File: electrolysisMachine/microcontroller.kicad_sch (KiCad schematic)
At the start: 1 part

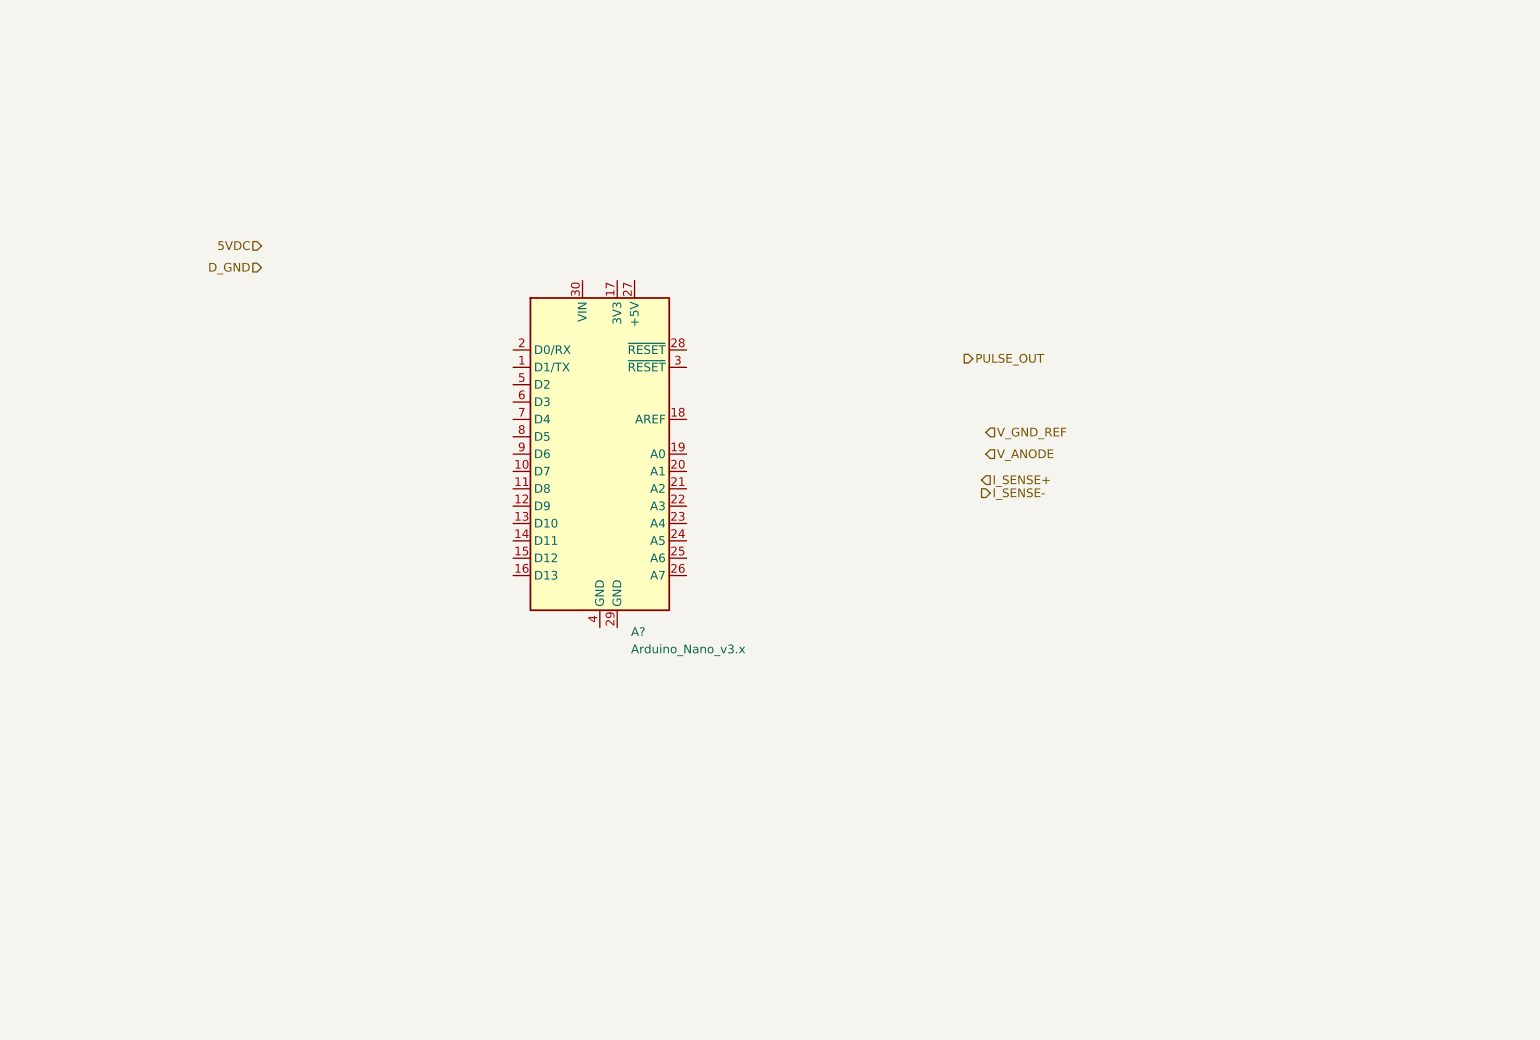
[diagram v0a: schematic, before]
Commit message: Added test circuit schematic
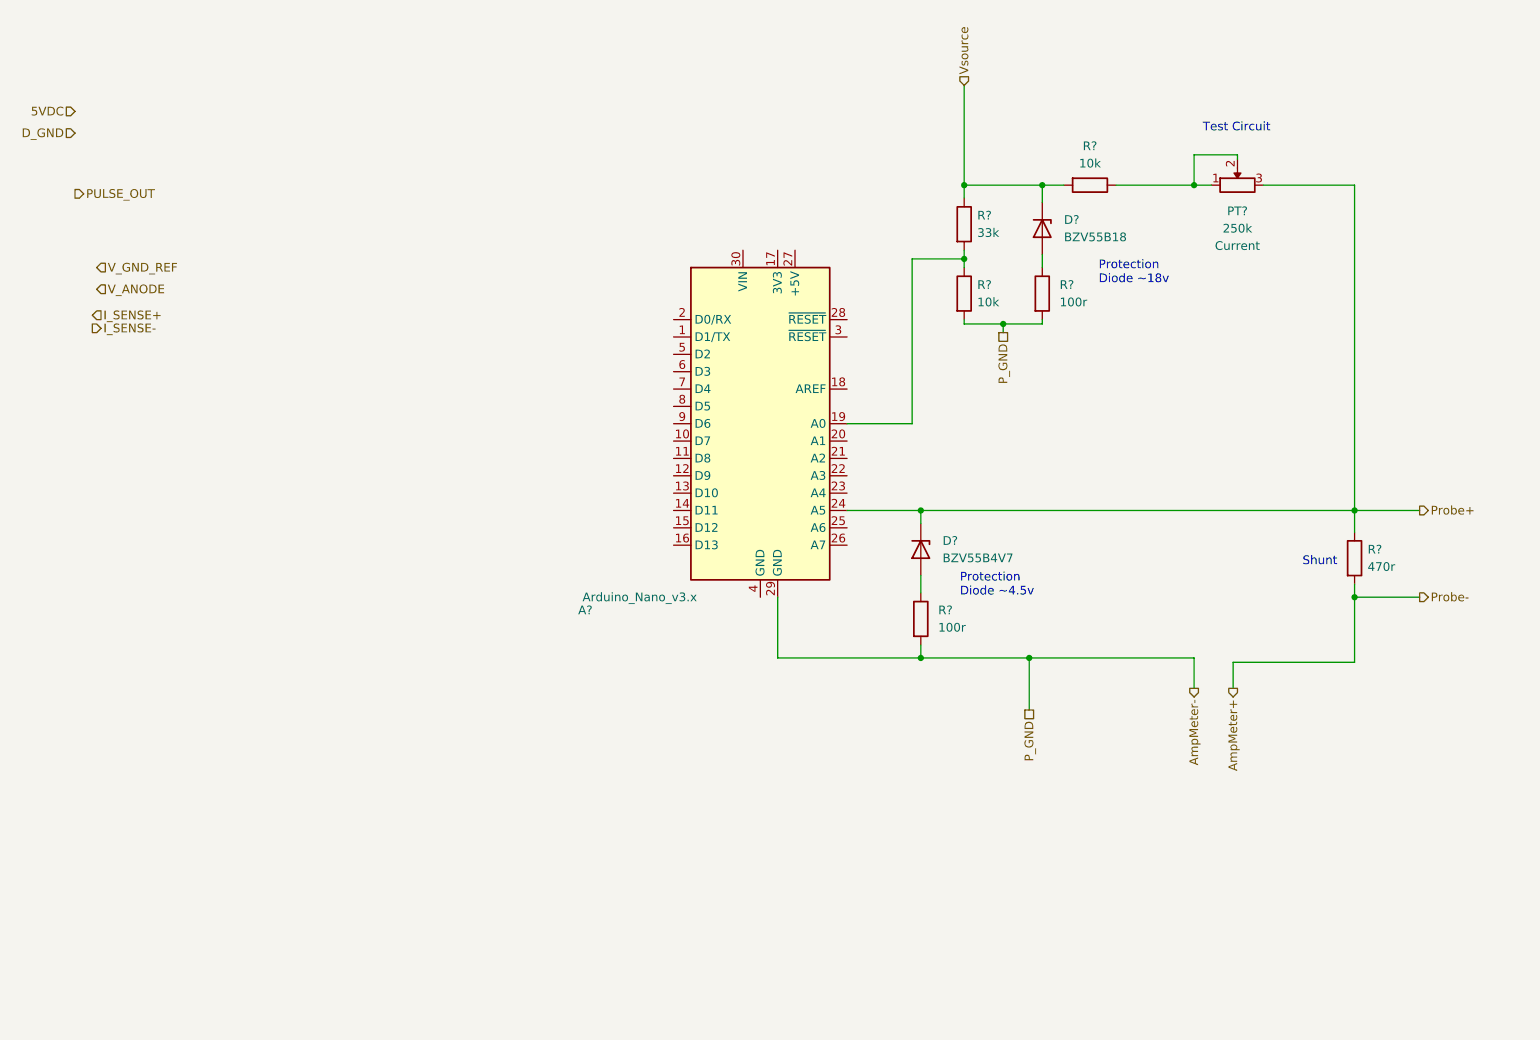
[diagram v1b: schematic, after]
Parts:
- added D?: BZV55B18, Diode_SMD:D_MiniMELF, symbol Diode:BZV55B18
- added D?: BZV55B4V7, Diode_SMD:D_MiniMELF, symbol Diode:BZV55B4V7
- added PT?: 250k, Potentiometer_THT:Potentiometer_Alpha_RD901F-40-00D_Single_Vertical_CircularHoles, symbol 000_Resistors_Immo:Potentiometer
- added R? (x2): 100r, Resistor_SMD:R_0805_2012Metric_Pad1.20x1.40mm_HandSolder, symbol 000_Resistors_Immo:Resistor_0805
- added R?: 470r, Resistor_SMD:R_0805_2012Metric_Pad1.20x1.40mm_HandSolder, symbol 000_Resistors_Immo:Resistor_0805
- added R? (x2): 10k, Resistor_SMD:R_0805_2012Metric_Pad1.20x1.40mm_HandSolder, symbol 000_Resistors_Immo:Resistor_0805
- added R?: 33k, Resistor_SMD:R_0805_2012Metric_Pad1.20x1.40mm_HandSolder, symbol 000_Resistors_Immo:Resistor_0805
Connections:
- net at A?.19 (A0): now also R?.1, R?.2
- net Probe+: now reaches A?.24 (A5)
- net Probe+: now also D?.1 (K), PT?.3, R?.1
- net AmpMeter-: now reaches A?.29 (GND)
- net AmpMeter-: now also R?.2, R?.2, R?.2
- new net: D?.2 (A), R?.1 (x2)
- new net: PT?.1, PT?.2, R?.1
- new net AmpMeter+: R?.2
- new net Vsource: D?.1 (K), R?.1, R?.2
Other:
- note added: "Protection Diode ~18v"
- note added: "Protection Diode ~4.5v"
- note added: "Shunt"
- note added: "Test Circuit"
- moved on the sheet: A?

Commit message: cgfhgfh
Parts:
- gave numbers to parts that had none: 10
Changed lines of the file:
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@@
   (symbol (lib_id "Diode:BZV55B18") (at 172.085 43.815 270) (unit 1)
     (in_bom yes) (on_board yes) (fields_autoplaced)
-    (property "Reference" "D?" (id 0) (at 175.26 42.5449 90)
+    (property "Reference" "D1" (id 0) (at 175.26 42.5449 90)
       (effects (font (size 1.27 1.27)) (justify left))
     )
@@
   (symbol (lib_id "000_Resistors_Immo:Resistor_0805") (at 172.085 53.34 270) (unit 1)
     (in_bom yes) (on_board yes) (fields_autoplaced)
-    (property "Reference" "R?" (id 0) (at 174.625 52.0699 90)
+    (property "Reference" "R4" (id 0) (at 174.625 52.0699 90)
       (effects (font (size 1.27 1.27)) (justify left))
     )
@@
   (symbol (lib_id "000_Resistors_Immo:Resistor_0805") (at 217.805 92.075 270) (unit 1)
     (in_bom yes) (on_board yes) (fields_autoplaced)
-    (property "Reference" "R?" (id 0) (at 219.71 90.8049 90)
+    (property "Reference" "R5" (id 0) (at 219.71 90.8049 90)
       (effects (font (size 1.27 1.27)) (justify left))
     )
@@
   (symbol (lib_id "000_Resistors_Immo:Resistor_0805") (at 154.305 100.965 270) (unit 1)
     (in_bom yes) (on_board yes) (fields_autoplaced)
-    (property "Reference" "R?" (id 0) (at 156.845 99.6949 90)
+    (property "Reference" "R6" (id 0) (at 156.845 99.6949 90)
       (effects (font (size 1.27 1.27)) (justify left))
     )
@@
   (symbol (lib_id "MCU_Module:Arduino_Nano_v3.x") (at 130.81 72.39 0) (unit 1)
     (in_bom yes) (on_board yes)
-    (property "Reference" "A?" (id 0) (at 104.14 99.695 0)
+    (property "Reference" "A1" (id 0) (at 104.14 99.695 0)
       (effects (font (size 1.27 1.27)) (justify left))
     )
@@
   (symbol (lib_id "000_Resistors_Immo:Resistor_0805") (at 179.07 37.465 180) (unit 1)
     (in_bom yes) (on_board yes) (fields_autoplaced)
-    (property "Reference" "R?" (id 0) (at 179.07 31.75 0))
+    (property "Reference" "R1" (id 0) (at 179.07 31.75 0))
     (property "Value" "10k" (id 1) (at 179.07 34.29 0))
     (property "Footprint" "Resistor_SMD:R_0805_2012Metric_Pad1.20x1.40mm_HandSolder" (id 2) (at 179.07 35.687 0)
@@
   (symbol (lib_id "000_Resistors_Immo:Resistor_0805") (at 160.655 43.18 270) (unit 1)
     (in_bom yes) (on_board yes) (fields_autoplaced)
-    (property "Reference" "R?" (id 0) (at 162.56 41.9099 90)
+    (property "Reference" "R2" (id 0) (at 162.56 41.9099 90)
       (effects (font (size 1.27 1.27)) (justify left))
     )
@@
   (symbol (lib_id "Diode:BZV55B4V7") (at 154.305 90.805 270) (unit 1)
     (in_bom yes) (on_board yes) (fields_autoplaced)
-    (property "Reference" "D?" (id 0) (at 157.48 89.5349 90)
+    (property "Reference" "D2" (id 0) (at 157.48 89.5349 90)
       (effects (font (size 1.27 1.27)) (justify left))
     )
@@
   (symbol (lib_id "000_Resistors_Immo:Resistor_0805") (at 160.655 53.34 270) (unit 1)
     (in_bom yes) (on_board yes) (fields_autoplaced)
-    (property "Reference" "R?" (id 0) (at 162.56 52.0699 90)
+    (property "Reference" "R3" (id 0) (at 162.56 52.0699 90)
       (effects (font (size 1.27 1.27)) (justify left))
     )
@@
   (symbol (lib_id "000_Resistors_Immo:Potentiometer") (at 200.66 37.465 90) (unit 1)
     (in_bom yes) (on_board yes) (fields_autoplaced)
-    (property "Reference" "PT?" (id 0) (at 200.66 41.275 90))
+    (property "Reference" "PT1" (id 0) (at 200.66 41.275 90))
     (property "Value" "250k" (id 1) (at 200.66 43.815 90))
     (property "Footprint" "Potentiometer_THT:Potentiometer_Alpha_RD901F-40-00D_Single_Vertical_CircularHoles" (id 2) (at 214.63 37.465 0)

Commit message: bjhvgj
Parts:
- removed D1: BZV55B18, Diode_SMD:D_MiniMELF, symbol Diode:BZV55B18
- removed PT1: 250k, Potentiometer_THT:Potentiometer_Alpha_RD901F-40-00D_Single_Vertical_CircularHoles, symbol 000_Resistors_Immo:Potentiometer
- removed R2: 33k, Resistor_SMD:R_0805_2012Metric_Pad1.20x1.40mm_HandSolder, symbol 000_Resistors_Immo:Resistor_0805
- removed R3: 10k, Resistor_SMD:R_0805_2012Metric_Pad1.20x1.40mm_HandSolder, symbol 000_Resistors_Immo:Resistor_0805
- removed R4: 100r, Resistor_SMD:R_0805_2012Metric_Pad1.20x1.40mm_HandSolder, symbol 000_Resistors_Immo:Resistor_0805
- added D?: BZV55B18, Diode_SMD:D_MiniMELF, symbol Diode:BZV55B18
- added D? (x4): LED, LED_SMD:LED_0805_2012Metric_Pad1.15x1.40mm_HandSolder, symbol Device:LED
- added D?: 1N4001, Diode_THT:D_DO-41_SOD81_P10.16mm_Horizontal, symbol Diode:1N4001
- added PT?: 100k, Potentiometer_THT:Potentiometer_Alpha_RD901F-40-00D_Single_Vertical_CircularHoles, symbol 000_Resistors_Immo:Potentiometer
- added Q?: BC547, Package_TO_SOT_THT:TO-92_Inline, symbol Transistor_BJT:BC547
- added R?: 3k3, Resistor_SMD:R_0805_2012Metric_Pad1.20x1.40mm_HandSolder, symbol 000_Resistors_Immo:Resistor_0805
- added R?: 4k7, Resistor_SMD:R_0805_2012Metric_Pad1.20x1.40mm_HandSolder, symbol 000_Resistors_Immo:Resistor_0805
- added R? (x3): 10k, Resistor_SMD:R_0805_2012Metric_Pad1.20x1.40mm_HandSolder, symbol 000_Resistors_Immo:Resistor_0805
- added R?: 220r, Resistor_SMD:R_0805_2012Metric_Pad1.20x1.40mm_HandSolder, symbol 000_Resistors_Immo:Resistor_0805
- added R?: 33k, Resistor_SMD:R_0805_2012Metric_Pad1.20x1.40mm_HandSolder, symbol 000_Resistors_Immo:Resistor_0805
- added R?: 100r, Resistor_SMD:R_0805_2012Metric_Pad1.20x1.40mm_HandSolder, symbol 000_Resistors_Immo:Resistor_0805
- added SW?: Trigger Output, symbol 000_Switches_Immo:pushbutton_tactile_4pin_th
- added SW?: Test Output, symbol 000_Switches_Immo:pushbutton_tactile_4pin_th
- R1: value 10k -> 8k2
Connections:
- net AmpMeter-: now also D?.1 (K), PT?.1, R?.2, R?.2, R?.2, R?.2, R?.2
- net Probe+: now also D?.1 (K); no longer A1.24 (A5), D2.1 (K), R5.1
- net Vsource: now also R1.1, D?.1 (K), D?.2 (A), R?.1; no longer R1.2
- net Vin_sense: now reaches A1.19 (A0)
- net Vin_sense: now also R?.1, R?.2
- net at A1.22 (A3): now also PT?.2
- net at A1.27 (+5V): now also PT?.3, R?.1, SW?.1, SW?.2
- net transistor_control: now reaches A1.6 (D3)
- net transistor_control: now also D?.2 (A)
- net at A1.9 (D6): now also R?.2, SW?.3 (K), SW?.4 (A)
- new net: D?.2 (A), R?.1
- new net: D?.1 (K), R?.1 (x2)
- new net: D?.1 (K), D?.2 (A), R?.1, SW?.3 (K), SW?.4 (A)
- new net: Q?.1 (C), R1.2
- new net: Q?.2 (B), R?.1, R?.2
- new net: D?.2 (A), Q?.3 (E)
- new net: D?.2 (A), SW?.1, SW?.2
- new net shunt_sense: A1.24 (A5), D2.1 (K), R5.1
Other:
- note added: "Arduino powered via USB"
- note added: "Connected for now"
- note added: "Power Input"
- note added: "Power Suppply: DC/DC Adjustable Buck Converter Module"
- note added: "Protection Diode ~4.5v Currently 5.1v"
- note added: "Sometimes Connected"
- note added: "Source Voltage 5-15v 18v MAX"
- note removed: "Protection Diode ~4.5v"
- moved on the sheet: A1, D2, R1, R5, R6
